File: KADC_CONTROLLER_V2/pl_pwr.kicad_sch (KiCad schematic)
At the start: 0 parts

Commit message: many updates
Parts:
- added C149, C150, C151, C152, C153, C154, C156, C157, C158, C162, C163, C164, C165, C166, C167, C171, C172, C173: 22u, Capacitor_SMD:C_0603_1608Metric, symbol Device:C_Small
- added C168, C170, C195, C197: 10u, Capacitor_SMD:C_0603_1608Metric, symbol Device:C_Small
- added C169, C196: 1000p, Capacitor_SMD:C_0603_1608Metric, symbol Device:C_Small
- added C198: 0.1u, Capacitor_SMD:C_0603_1608Metric, symbol Device:C_Small
- added R139, R140, R155: 40.2k, Resistor_SMD:R_0603_1608Metric, symbol Device:R_Small_US
- added R141: 60k, Resistor_SMD:R_0603_1608Metric, symbol Device:R_Small_US
- added R142: 30k, Resistor_SMD:R_0603_1608Metric, symbol Device:R_Small_US
- added R143: 80k, Resistor_SMD:R_0603_1608Metric, symbol Device:R_Small_US
- added R144: 25k, Resistor_SMD:R_0603_1608Metric, symbol Device:R_Small_US
- added R147, R148, R149, R150, R151, R156, R178, R179: 100k, Resistor_SMD:R_0603_1608Metric, symbol Device:R_Small_US
- added R152: 49.9k, Resistor_SMD:R_0603_1608Metric, symbol Device:R_Small_US
- added R153, R154, R177: 10k, Resistor_SMD:R_0603_1608Metric, symbol Device:R_Small_US
- added R157: 200k, Resistor_SMD:R_0603_1608Metric, symbol Device:R_Small_US
- added R158: 44,2k, Resistor_SMD:R_0603_1608Metric, symbol Device:R_Small_US
- added U30, U31, U32: MPM3810AGQB-AEC1-Z, QFN-12_MPM3810_MNP, symbol MPM3810AGQB0AEC1-Z:MPM3810AGQB-AEC1-Z
- added U34, U35, U37: TPSM82866AA0SRDJR, RDJ0023A-MFG, symbol TPSM82866AA0SRDJR:TPSM82866AA0SRDJR
- added U36: NC7WZ07L6X, MICROPAK6_1X1P45_ONS, symbol NC7WZ07L6X:NC7WZ07L6X
- added U50, U51: MP8904DD-LF-Z, QFN8_MNP, symbol MP8904DD-LF-Z:MP8904DD-LF-Z
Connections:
- new net: R151.2, R152.1, U35.17 (FB)
- new net: C169.1, R153.2, R154.1, U50.4 (FB)
- new net: R157.2, R158.1, U37.17 (FB)
- new net: R139.2, R140.1, U30.10 (FB)
- new net: C196.1, R155.2, R177.1, U51.4 (FB)
- new net: R141.2, R142.1, U31.10 (FB)
- new net: R147.2, R148.1, U34.17 (FB)
- new net: R143.2, R144.1, U32.10 (FB)
- new net 5V0_IN: C149.2, C152.2, C156.2, C162.2, C165.2, C171.2, C198.2, R149.1, R150.1, R156.1, R178.1, U30.7 (VIN), U31.7 (VIN), U32.7 (VIN), U34.21 (VIN), U34.22 (VIN), U34.3 (VSET_MODE), U35.21 (VIN), U35.22 (VIN), U35.3 (VSET_MODE), U36.5 (VCC), U37.21 (VIN), U37.22 (VIN), U37.3 (VSET_MODE)
- new net CC_PL_PGOOD: U30.8 (PG), U31.8 (PG), U32.8 (PG)
- new net CC_PS_PGOOD: R149.2, R150.2, U34.2 (PG), U35.2 (PG), U36.4 (Y2), U50.3 (PG), U51.3 (PG)
- new net ETH_1V0: C169.2, C170.2, R153.1, U50.1 (OUT)
- new net ETH_2V5: C196.2, C197.2, R155.1, U51.1 (OUT)
- new net ETH_REG_EN: R179.2, U36.6 (Y1), U50.5 (EN), U51.5 (EN)
- new net GND: C149.1, C150.1, C151.1, C152.1, C153.1, C154.1, C156.1, C157.1, C158.1, C162.1, C163.1, C164.1, C165.1, C166.1, C167.1, C168.1, C170.1, C171.1, C172.1, C173.1, C195.1, C197.1, C198.1, R140.2, R142.2, R144.2, R148.2, R152.2, R154.2, R158.2, R177.2, U30.1 (PGND), U30.11 (AGND), U30.2 (PGND), U31.1 (PGND), U31.11 (AGND), U31.2 (PGND), U32.1 (PGND), U32.11 (AGND), U32.2 (PGND), U34.10 (PGND), U34.11 (PGND), U34.18 (AGND), U34.19 (PGND), U34.20 (PGND), U34.23 (PGND), U34.4 (PGND), U34.5 (PGND), U34.6 (PGND), U34.8 (PGND), U34.9 (PGND), U35.10 (PGND), U35.11 (PGND), U35.18 (AGND), U35.19 (PGND), U35.20 (PGND), U35.23 (PGND), U35.4 (PGND), U35.5 (PGND), U35.6 (PGND), U35.8 (PGND), U35.9 (PGND), U36.2 (GND), U37.10 (PGND), U37.11 (PGND), U37.18 (AGND), U37.19 (PGND), U37.20 (PGND), U37.23 (PGND), U37.4 (PGND), U37.5 (PGND), U37.6 (PGND), U37.8 (PGND), U37.9 (PGND), U50.6 (GND), U50.9 (GND), U51.6 (GND), U51.9 (GND)
- new net PL_1V2: C150.2, C151.2, R139.1, U30.12 (OUT_S), U30.5 (OUT), U30.6 (OUT)
- new net PL_1V8: C153.2, C154.2, R141.1, U31.12 (OUT_S), U31.5 (OUT), U31.6 (OUT)
- new net PL_2V5: C157.2, C158.2, R143.1, U32.12 (OUT_S), U32.5 (OUT), U32.6 (OUT)
- new net PS_1V2: C163.2, C164.2, R147.1, U34.12 (VOUT), U34.13 (VOUT), U34.14 (VOUT), U34.15 (VOUT), U34.16 (VOS)
- new net PS_1V8: C166.2, C167.2, R151.1, U35.12 (VOUT), U35.13 (VOUT), U35.14 (VOUT), U35.15 (VOUT), U35.16 (VOS)
- new net PS_3V3: C168.2, C172.2, C173.2, C195.2, R157.1, R179.1, U37.12 (VOUT), U37.13 (VOUT), U37.14 (VOUT), U37.15 (VOUT), U37.16 (VOS), U50.8 (IN), U51.8 (IN)
- new net PS_3V3_PGOOD: R156.2, R178.2, U36.1 (A1), U36.3 (A2), U37.2 (PG)
- new net VCCOEN_PL_M2C: U30.9 (EN), U31.9 (EN), U32.9 (EN)
- new net VCCOEN_PS_M2C: U34.1 (EN), U35.1 (EN), U37.1 (EN)
- no-connect marks 0 -> 3
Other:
- note added: "1.0V Ethernet"
- note added: "1.2V PL RAIL"
- note added: "1.2V PS RAIL"
- note added: "1.8V PL RAIL"
- note added: "1.8V PS RAIL"
- note added: "2.5V Ethernet"
- note added: "2.5V PL RAIL"
- note added: "3.3V PS RAIL"
- note added: "MPM3810 Resistive Divider Calculation"

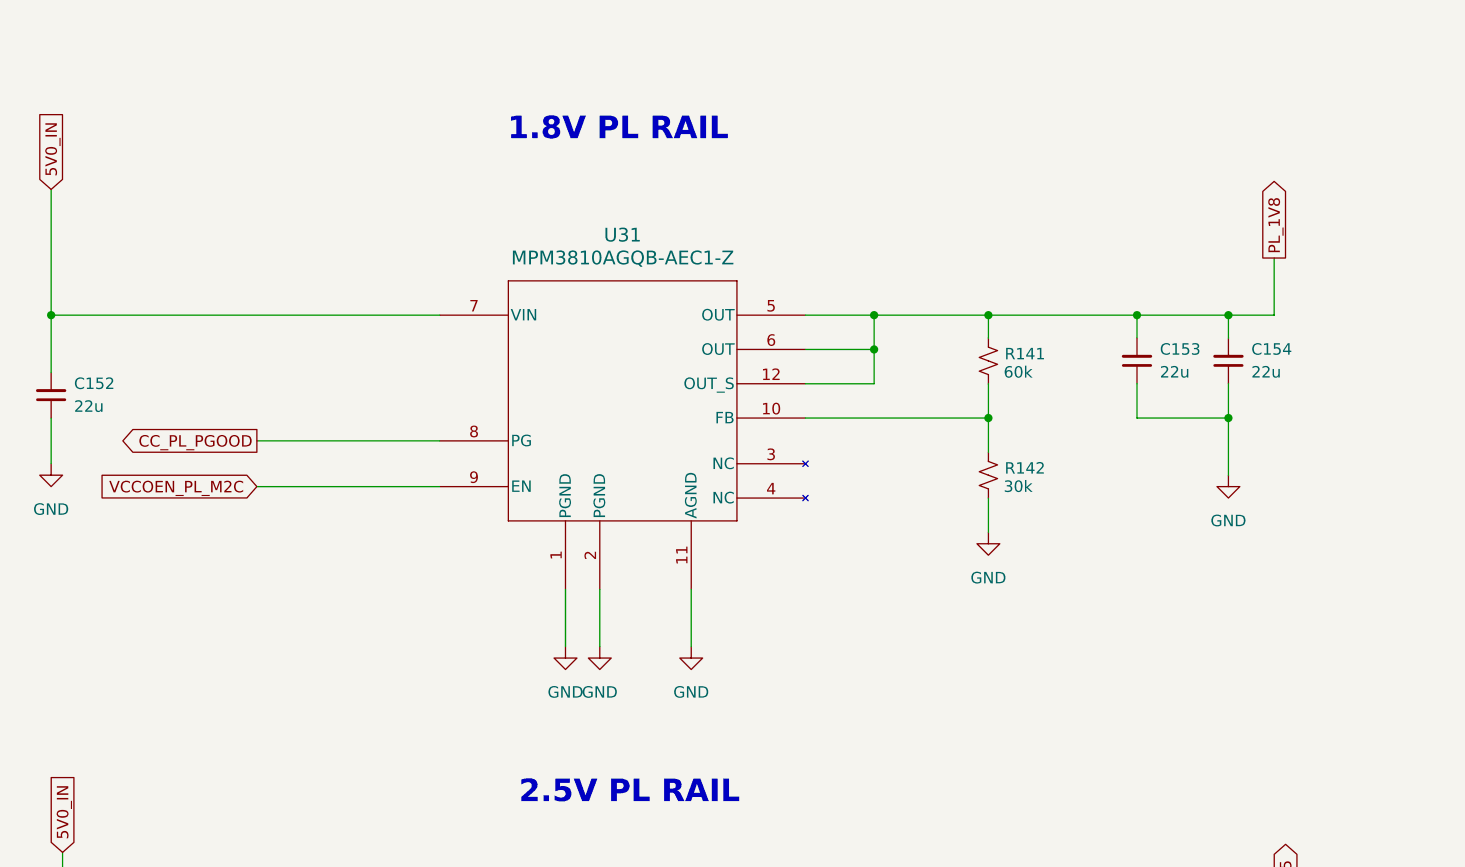
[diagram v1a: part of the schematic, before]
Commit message: Added footprints, updated schematic
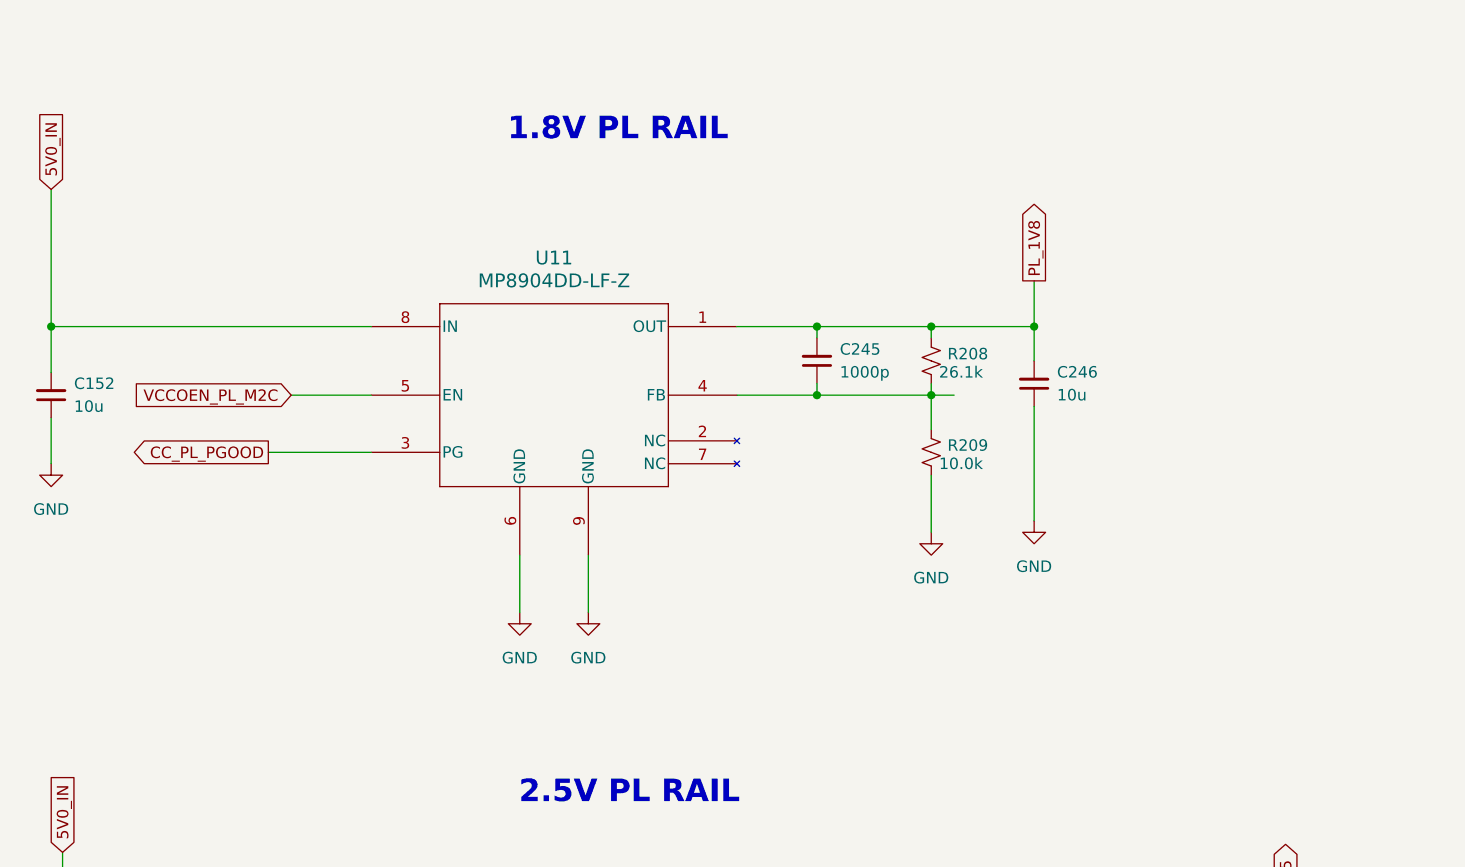
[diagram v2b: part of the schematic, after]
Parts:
- removed C153, C154: 22u, Capacitor_SMD:C_0603_1608Metric, symbol Device:C_Small
- removed R141: 60k, Resistor_SMD:R_0603_1608Metric, symbol Device:R_Small_US
- removed R142: 30k, Resistor_SMD:R_0603_1608Metric, symbol Device:R_Small_US
- removed U31: MPM3810AGQB-AEC1-Z, QFN-12_MPM3810_MNP, symbol MPM3810AGQB0AEC1-Z:MPM3810AGQB-AEC1-Z
- added C245: 1000p, Capacitor_SMD:C_0603_1608Metric, symbol Device:C_Small
- added C246: 10u, Capacitor_SMD:C_0603_1608Metric, symbol Device:C_Small
- added R208: 26.1k, Resistor_SMD:R_0603_1608Metric, symbol Device:R_Small_US
- added R209: 10.0k, Resistor_SMD:R_0603_1608Metric, symbol Device:R_Small_US
- added U11: MP8904DD-LF-Z, QFN8_MNP, symbol MP8904DD-LF-Z:MP8904DD-LF-Z
- C152: value 22u -> 10u
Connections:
- net 5V0_IN: now also U11.8 (IN)
- net CC_PL_PGOOD: now also U11.3 (PG)
- net GND: now also C246.1, R209.2, U11.6 (GND), U11.9 (GND)
- net PL_1V8: now also C245.2, C246.2, R208.1, U11.1 (OUT)
- net VCCOEN_PL_M2C: now also U11.5 (EN)
- new net: C245.1, R208.2, R209.1, U11.4 (FB)

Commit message: Updated Transistors
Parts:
- added R210: 10k, Resistor_SMD:R_0603_1608Metric, symbol Device:R_Small_US
- added TP37: ETH_PGOOD, TestPoint:TestPoint_THTPad_1.5x1.5mm_Drill0.7mm, symbol Connector:TestPoint
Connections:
- net CC_PS_PGOOD: no longer U50.3 (PG), U51.3 (PG)
- net PS_3V3: now also R210.1
- new net ETH_PGOOD: R210.2, TP37.1, U50.3 (PG), U51.3 (PG)

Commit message: Reupdate for verify
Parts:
- removed R149, R150: 100k, Resistor_SMD:R_0603_1608Metric, symbol Device:R_Small_US
- added R211, R212: 100k, Resistor_SMD:R_0603_1608Metric, symbol Device:R_Small_US
- added TP38: CC_PL_PGOOD, TestPoint:TestPoint_THTPad_1.5x1.5mm_Drill0.7mm, symbol Connector:TestPoint
- added TP39: CC_PS_PGOOD, TestPoint:TestPoint_THTPad_1.5x1.5mm_Drill0.7mm, symbol Connector:TestPoint
- U11, U50, U51: footprint QFN8_MNP -> MP8904DD_LF_Z:QFN8_MNP
- U30, U32: footprint QFN-12_MPM3810_MNP -> MPM3810AGQB_AEC1_Z:QFN-12_MPM3810_MNP
- U34, U35, U37: footprint RDJ0023A-MFG -> TPSM82866AA0SRDJR:RDJ0023A-SMD-MFG
- U36: footprint MICROPAK6_1X1P45_ONS -> NC7WZ07L6X:MICROPAK6_1X1P45_ONS
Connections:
- net 5V0_IN: now also R211.1, R212.1
- net CC_PL_PGOOD: now also R211.2, TP38.1
- net CC_PS_PGOOD: now also R212.2, TP39.1
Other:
- moved on the sheet: R210, TP37

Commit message: update for verification
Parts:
- removed R156: 100k, Resistor_SMD:R_0603_1608Metric, symbol Device:R_Small_US
- removed R210: 10k, Resistor_SMD:R_0603_1608Metric, symbol Device:R_Small_US
- removed TP37: ETH_PGOOD, TestPoint:TestPoint_THTPad_1.5x1.5mm_Drill0.7mm, symbol Connector:TestPoint
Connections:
- net ETH_PGOOD is gone; now on net CC_PS_PGOOD: U50.3 (PG), U51.3 (PG)
